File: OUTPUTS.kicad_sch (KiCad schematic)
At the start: 51 parts, among them J8 LED_OUT_CONN, J9 LED_OUT_CONN, U17 EL817, U18 EL817, U19 EL817, U20 EL817, U21 EL817, U22 EL817, U23 EL817, U24 EL817, U25 EL817, U26 EL817, U27 74HC04, U28 74HC04, U29 ULN2003A, U30 ULN2003A

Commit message: Specefies which section is complete and incomplete
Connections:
- net COMMON renamed COMMON_OUT
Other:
- moved on the sheet: C27, C37, J9, RN3, RN4, RN5, U27G, U28G

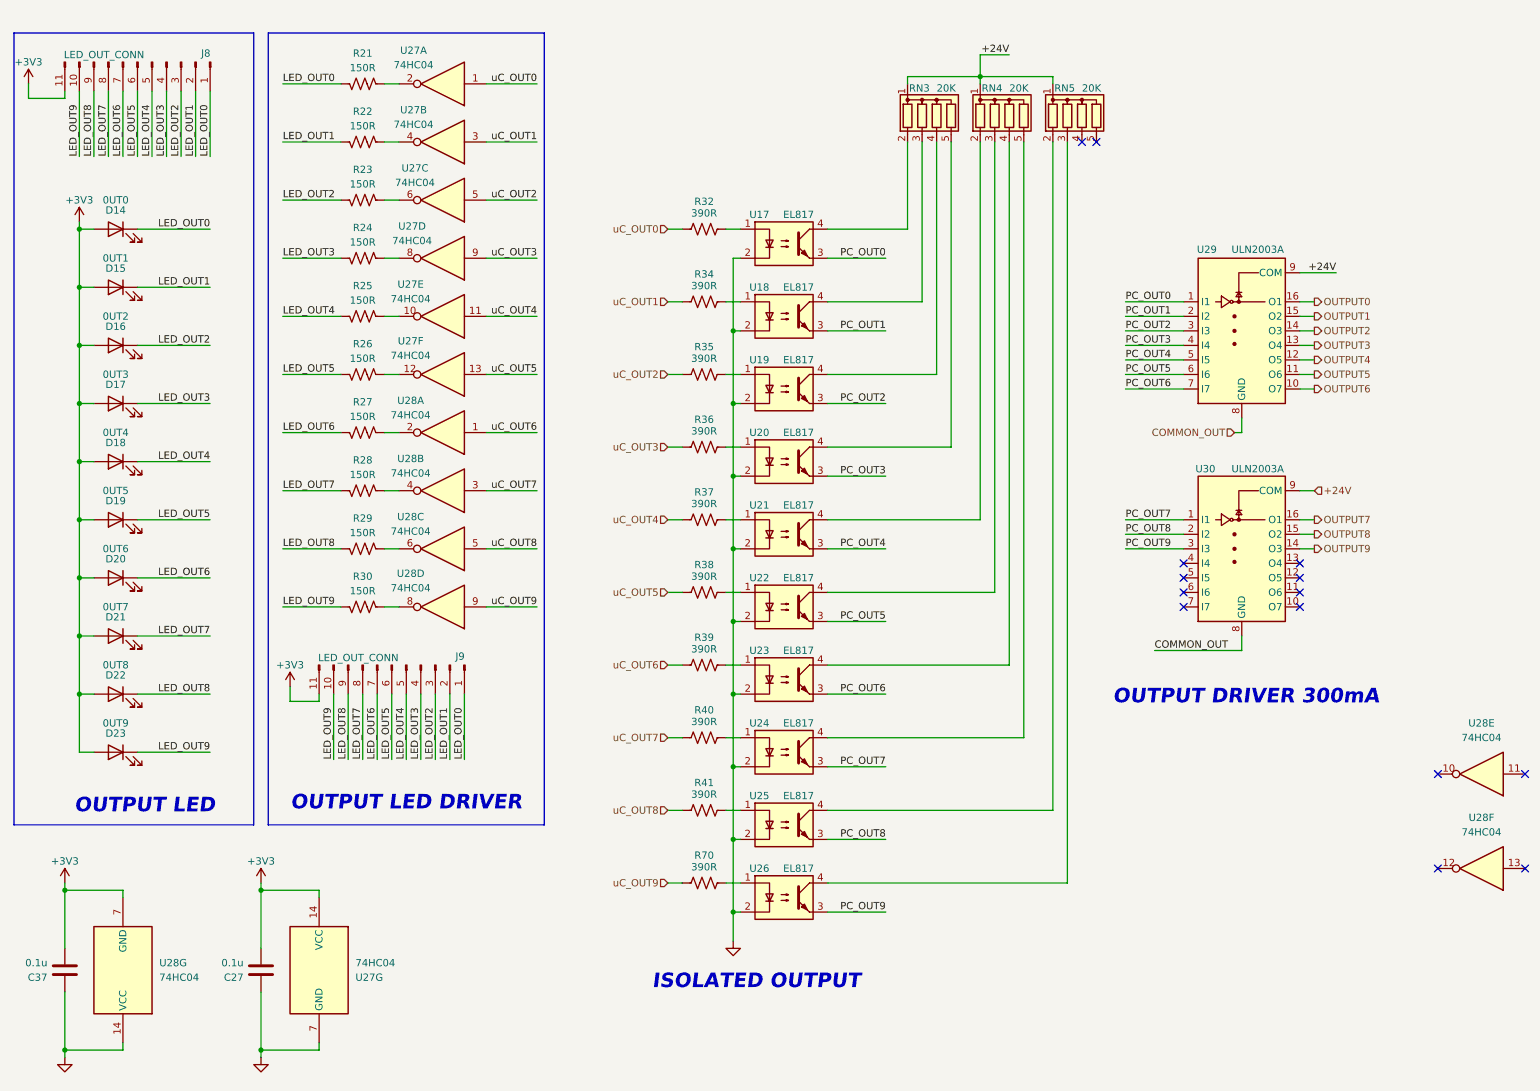
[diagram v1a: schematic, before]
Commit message: OUTPUT Sch. 74LHC125 added for buffered output
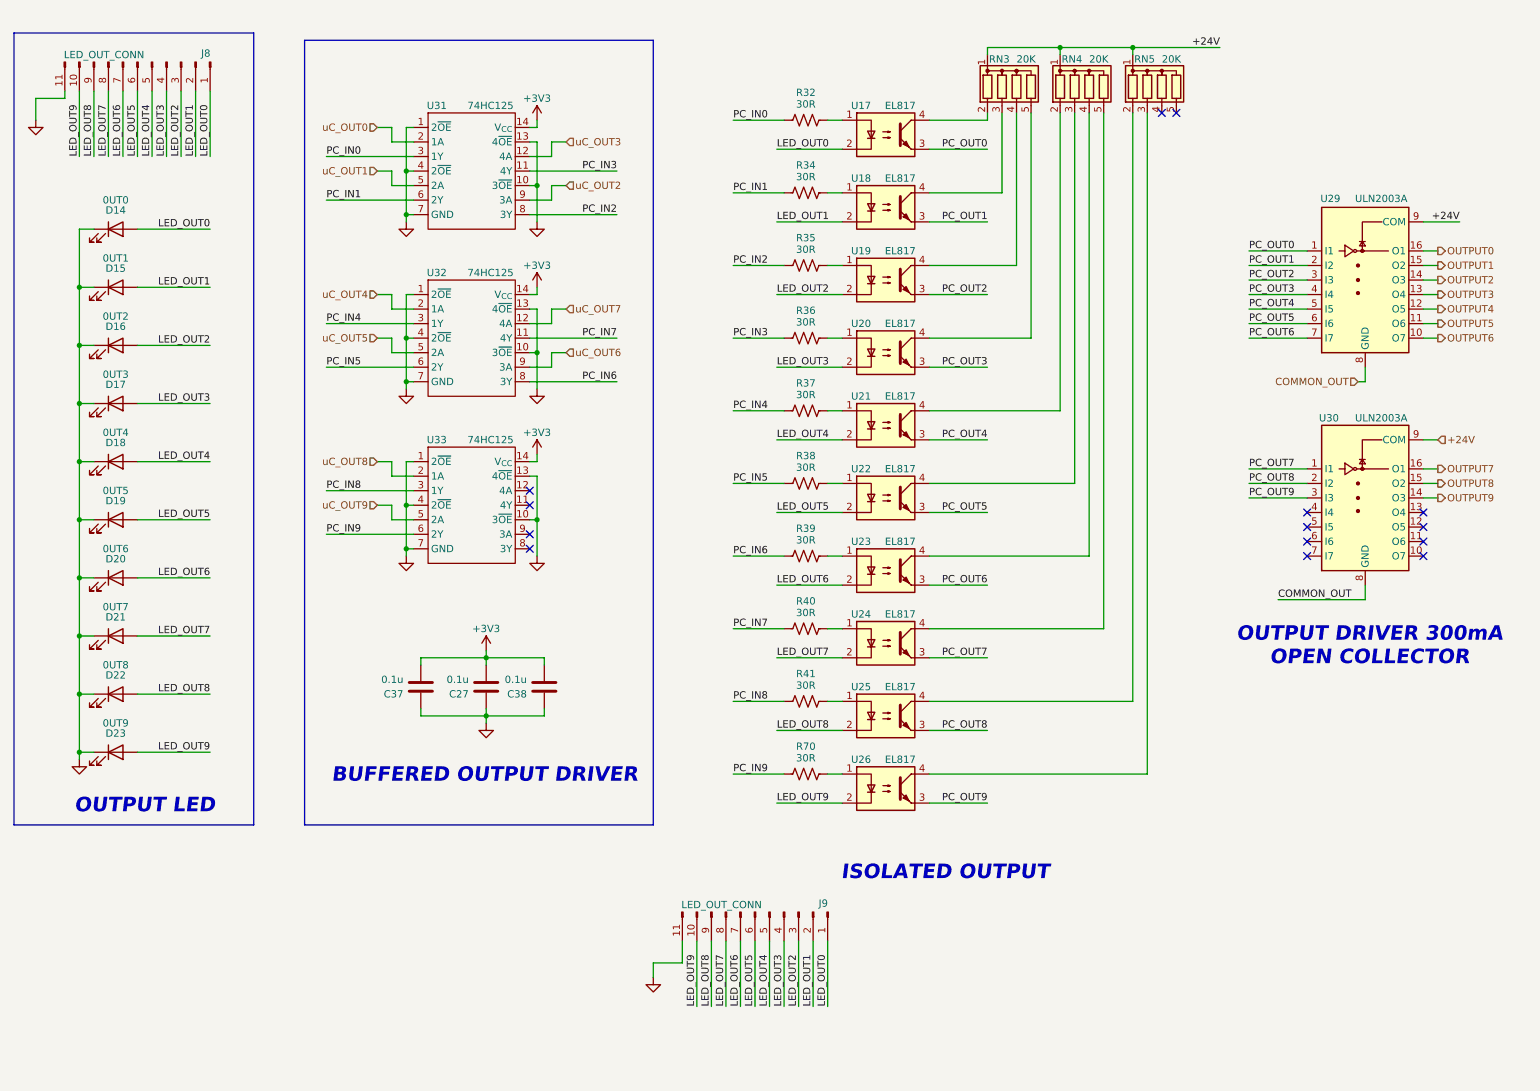
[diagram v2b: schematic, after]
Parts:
- removed R21, R22, R23, R24, R25, R26, R27, R28, R29, R30: 150R, Resistor_SMD:R_0603_1608Metric_Pad0.98x0.95mm_HandSolder, symbol Device:R_US
- removed U27, U28: 74HC04, Package_SO:SO-14_3.9x8.65mm_P1.27mm, symbol 74xx:74HC04
- added C38: 0.1u, Capacitor_SMD:C_0603_1608Metric_Pad1.08x0.95mm_HandSolder, symbol Device:C
- added U31, U32, U33: 74HC125, Package_SO:SOIC-14_3.9x8.7mm_P1.27mm, symbol 74HC125:74HC125
- R32, R34, R35, R36, R37, R38, R39, R40, R41, R70: value 390R -> 30R
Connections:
- net +3V3: now also C38.2, U31.14 (V_{CC}), U32.14 (V_{CC}), U33.14 (V_{CC}); no longer D14.2 (A), D15.2 (A), D16.2 (A), D17.2 (A), D18.2 (A), D19.2 (A), D20.2 (A), D21.2 (A), D22.2 (A), D23.2 (A), J8.11 (Pin_11), J9.11 (Pin_11)
- net GND: now also D14.1 (K), D15.1 (K), D16.1 (K), D17.1 (K), D18.1 (K), D19.1 (K), D20.1 (K), D21.1 (K), D22.1 (K), D23.1 (K), J8.11 (Pin_11), J9.11 (Pin_11), C38.1, U31.1 (2~{OE}), U31.10 (3~{OE}), U31.13 (4~{OE}), U31.4 (2~{OE}), U31.7 (GND), U32.1 (2~{OE}), U32.10 (3~{OE}), U32.13 (4~{OE}), U32.4 (2~{OE}), U32.7 (GND), U33.1 (2~{OE}), U33.10 (3~{OE}), U33.13 (4~{OE}), U33.4 (2~{OE}), U33.7 (GND); no longer U17.2, U18.2, U19.2, U20.2, U21.2, U22.2, U23.2, U24.2, U25.2, U26.2
- net LED_OUT0: now also D14.2 (A), U17.2; no longer D14.1 (K)
- net LED_OUT1: now also D15.2 (A), U18.2; no longer D15.1 (K)
- net LED_OUT2: now also D16.2 (A), U19.2; no longer D16.1 (K)
- net LED_OUT3: now also D17.2 (A), U20.2; no longer D17.1 (K)
- net LED_OUT4: now also D18.2 (A), U21.2; no longer D18.1 (K)
- net LED_OUT5: now also D19.2 (A), U22.2; no longer D19.1 (K)
- net LED_OUT6: now also D20.2 (A), U23.2; no longer D20.1 (K)
- net LED_OUT7: now also D21.2 (A), U24.2; no longer D21.1 (K)
- net LED_OUT8: now also D22.2 (A), U25.2; no longer D22.1 (K)
- net LED_OUT9: now also D23.2 (A), U26.2; no longer D23.1 (K)
- net uC_OUT0: now also U31.2 (1A); no longer R32.1
- net uC_OUT1: now also U31.5 (2A); no longer R34.1
- net uC_OUT2: now also U31.9 (3A); no longer R35.1
- net uC_OUT3: now also U31.12 (4A); no longer R36.1
- net uC_OUT4: now also U32.2 (1A); no longer R37.1
- net uC_OUT5: now also U32.5 (2A); no longer R38.1
- net uC_OUT6: now also U32.9 (3A); no longer R39.1
- net uC_OUT7: now also U32.12 (4A); no longer R40.1
- net uC_OUT8: now also U33.2 (1A); no longer R41.1
- net uC_OUT9: now also U33.5 (2A); no longer R70.1
- new net PC_IN0: R32.1, U31.3 (1Y)
- new net PC_IN1: R34.1, U31.6 (2Y)
- new net PC_IN2: R35.1, U31.8 (3Y)
- new net PC_IN3: R36.1, U31.11 (4Y)
- new net PC_IN4: R37.1, U32.3 (1Y)
- new net PC_IN5: R38.1, U32.6 (2Y)
- new net PC_IN6: R39.1, U32.8 (3Y)
- new net PC_IN7: R40.1, U32.11 (4Y)
- new net PC_IN8: R41.1, U33.3 (1Y)
- new net PC_IN9: R70.1, U33.6 (2Y)
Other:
- note added: "BUFFERED OUTPUT DRIVER"
- note added: "OUTPUT DRIVER 300mA OPEN COLLECTOR"
- note removed: "OUTPUT DRIVER 300mA"
- note removed: "OUTPUT LED DRIVER"
- moved on the sheet: C27, C37, D14, D15, D16, D17, D18, D19, D20, D21, D22, D23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
